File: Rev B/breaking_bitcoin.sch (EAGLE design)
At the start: 66 parts, among them J1 M20-9992046, J2 M20-9992046, J3 M20-9992046, J4 TC2050-IDC-NLFP, J5 DNP, J6 DNP, J7 ZX80-B-5P, Q1 DMG2302UK, U1 STM32F205RE, U2 MCP1703AT-3302E/CB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

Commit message: Fixing south bridge for the Rev. B
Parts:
- added JP1: JUMPER-PAD-2-NC_BY_TRACE, SparkFun-Passives:JUMPER-PAD-2-NC_BY_TRACE
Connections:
- new net N$12: J3.P$20, JP1.1
- net 3.3V: now also JP1.2; no longer J3.P$20
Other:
- note added: "OLED Test Points (Compatible w HiLetgo 3-01-1234-W)"
- note removed: "OLED Test Points"
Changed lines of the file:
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@@
 <part name="U$2" library="KVB-misc" deviceset="CRYPTOTRONIX_LOGO" device=""/>
 <part name="U$3" library="KVB-misc" deviceset="BB_LOGO" device=""/>
+<part name="JP1" library="SparkFun-Passives" deviceset="JUMPER-PAD-2-NC_BY_TRACE" device=""/>
 </parts>
 <sheets>
@@
 Permanently
 set to 1.2V</text>
-<text x="213.36" y="101.6" size="1.778" layer="95">CW_LED3
+<text x="213.36" y="99.06" size="1.778" layer="95">CW_LED3
 indicates
 power is ON!</text>
-<text x="187.96" y="58.42" size="1.778" layer="95">OLED Test Points</text>
+<text x="187.96" y="58.42" size="1.778" layer="95">OLED Test Points
+(Compatible w HiLetgo 3-01-1234-W)</text>
 </plain>
 <instances>
@@
 <instance part="U$1" gate="G$1" x="220.98" y="48.26"/>
 <instance part="U$2" gate="G$1" x="215.9" y="25.4"/>
+<instance part="JP1" gate="G$1" x="220.98" y="109.22" smashed="yes">
+<attribute name="NAME" x="213.36" y="109.22" size="1.778" layer="95"/>
+</instance>
 </instances>
 <busses>
@@
 </segment>
 <segment>
-<pinref part="J3" gate="G$1" pin="P$20"/>
 <pinref part="3.3V6" gate="G$1" pin="3.3V"/>
-<wire x1="198.12" y1="109.22" x2="231.14" y2="109.22" width="0.1524" layer="91"/>
 <wire x1="231.14" y1="109.22" x2="231.14" y2="114.3" width="0.1524" layer="91"/>
+<pinref part="JP1" gate="G$1" pin="2"/>
+<wire x1="226.06" y1="109.22" x2="231.14" y2="109.22" width="0.1524" layer="91"/>
 </segment>
 <segment>
@@
 </segment>
 </net>
+<net name="N$12" class="0">
+<segment>
+<pinref part="J3" gate="G$1" pin="P$20"/>
+<pinref part="JP1" gate="G$1" pin="1"/>
+<wire x1="198.12" y1="109.22" x2="215.9" y2="109.22" width="0.1524" layer="91"/>
+</segment>
+</net>

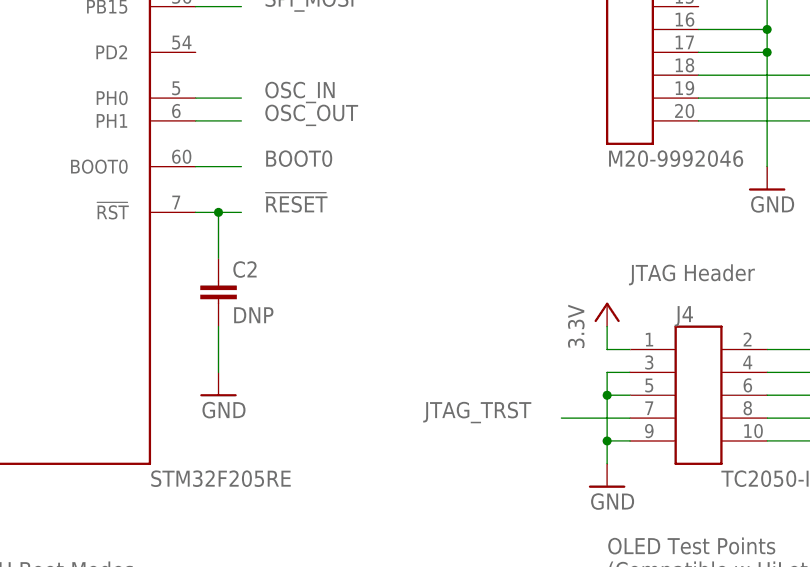
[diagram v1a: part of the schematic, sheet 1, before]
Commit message: Adding reset MCU hint notes
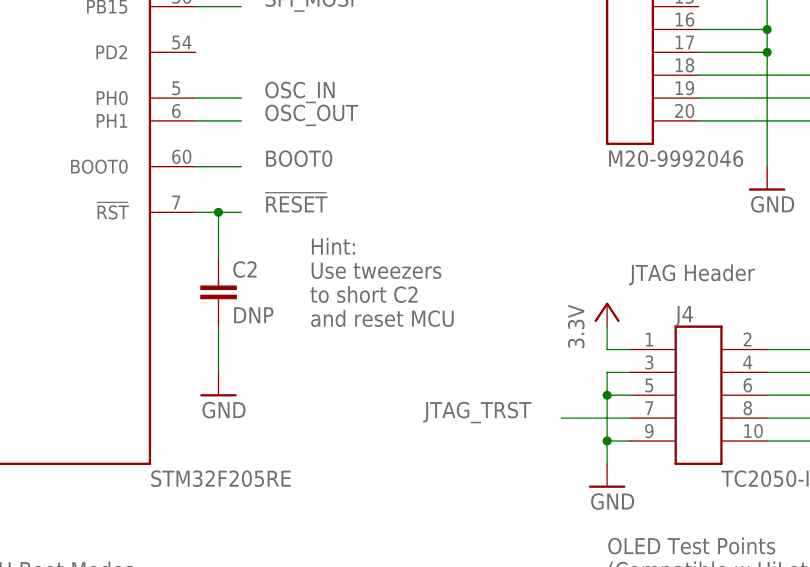
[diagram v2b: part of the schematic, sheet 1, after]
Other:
- note added: "Hint: Use tweezers to short C2 and reset MCU"
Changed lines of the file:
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@@
 <setting verticaltext="up"/>
 </settings>
-<grid distance="0.1" unitdist="inch" unit="inch" style="lines" multiple="1" display="yes" altdistance="0.01" altunitdist="inch" altunit="inch"/>
+<grid distance="0.1" unitdist="inch" unit="inch" style="lines" multiple="1" display="no" altdistance="0.01" altunitdist="inch" altunit="inch"/>
 <layers>
 <layer number="1" name="Top" color="4" fill="1" visible="no" active="no"/>
@@
 <text x="187.96" y="58.42" size="1.778" layer="95">OLED Test Points
 (Compatible w HiLetgo 3-01-1234-W)</text>
+<text x="154.94" y="86.36" size="1.778" layer="95">Hint:
+Use tweezers
+to short C2
+and reset MCU</text>
 </plain>
 <instances>
